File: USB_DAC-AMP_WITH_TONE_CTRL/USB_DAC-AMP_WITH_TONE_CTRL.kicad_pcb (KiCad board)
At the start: 2 copper layers, 9 parts, among them J2 SJ-3524-SMT, U1 PCM2906, U2 TPS61040DBV, U3 SPX3819M5-L, U4 SPX3819M5-L

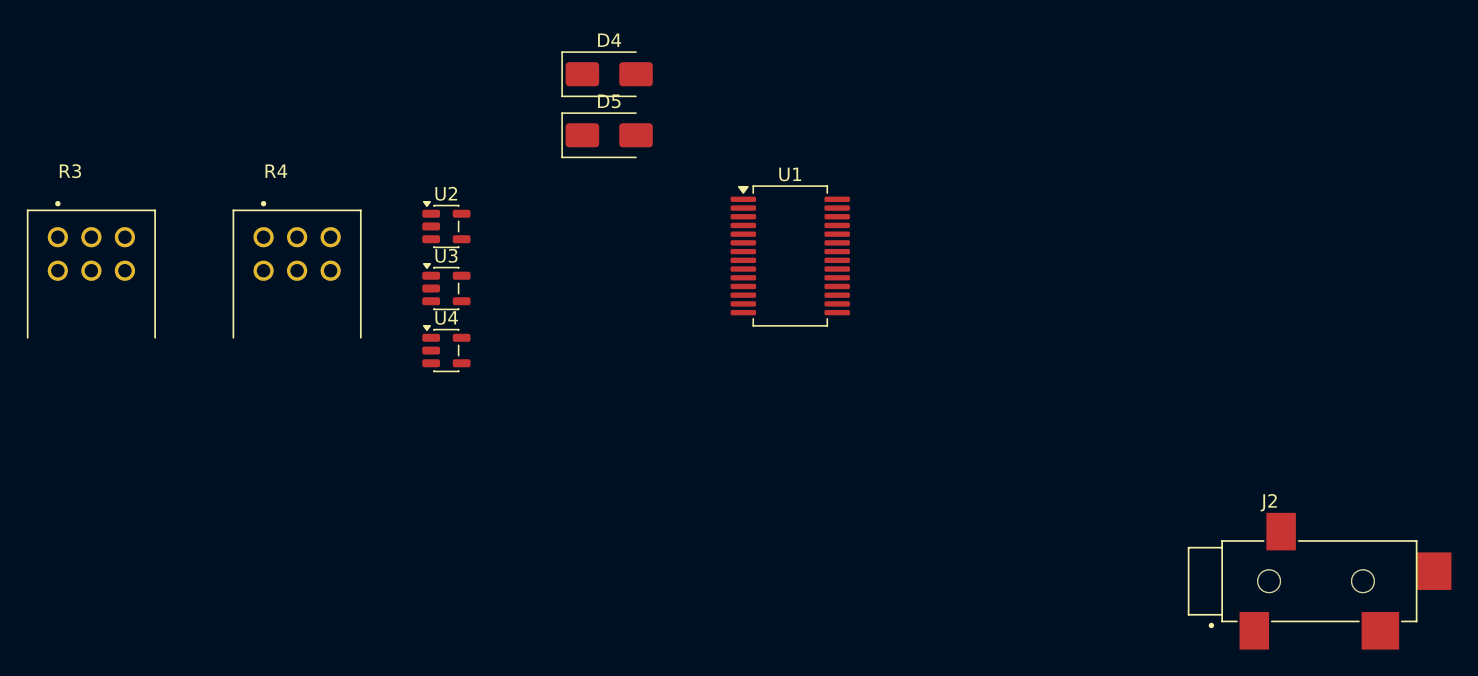
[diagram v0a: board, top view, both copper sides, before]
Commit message: finished USB_DAC-AMP schematic
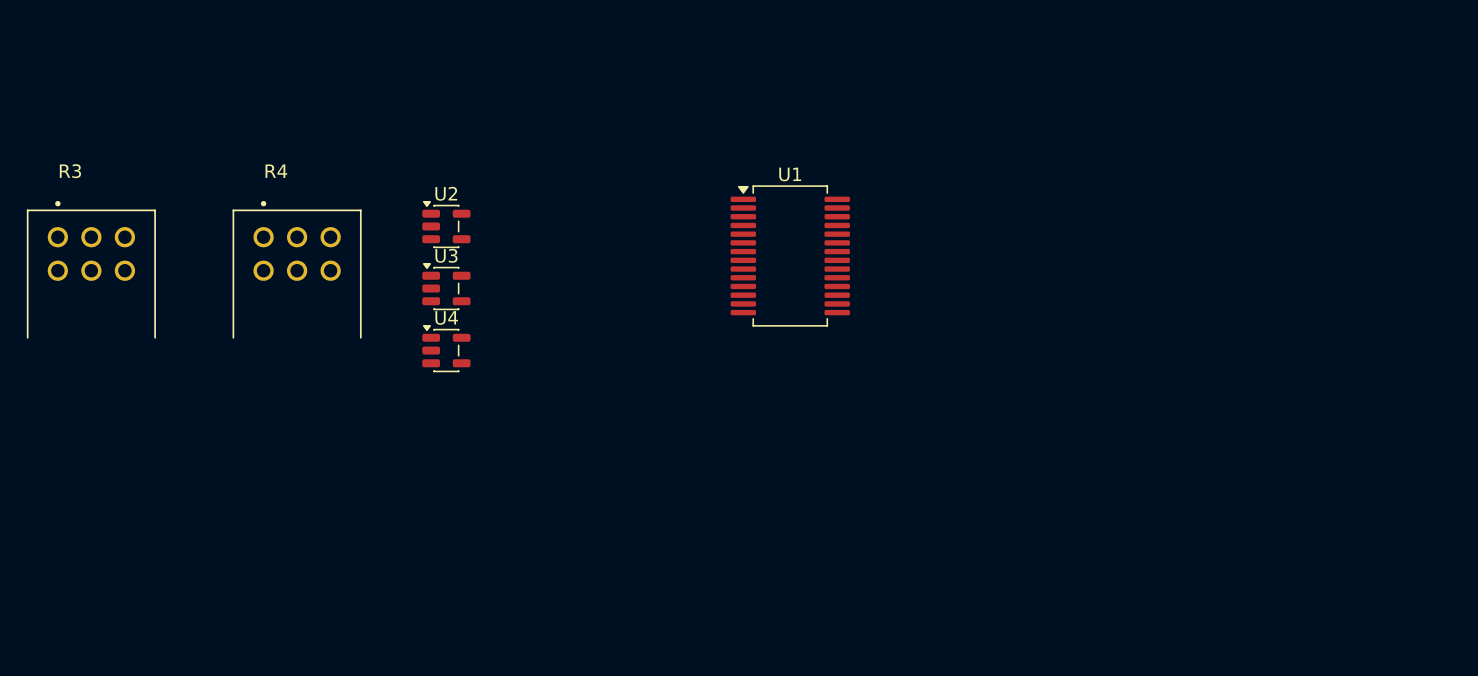
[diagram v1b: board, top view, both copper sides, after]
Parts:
- removed D4, D5: SS14, Diode_SMD:D_SMA
- removed J2: SJ-3524-SMT, Imported_footprints:SJ-3524-SMT
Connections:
- R3 pad 1_1: Net-(C30-Pad2) -> unconnected-(R3-Pad1_1)
- R3 pad 1_2: Net-(C40-Pad2) -> unconnected-(R3-Pad1_2)
- R3 pad 2_1: Net-(C31-Pad2) -> unconnected-(R3-Pad2_1)
- R3 pad 2_2: Net-(C41-Pad2) -> unconnected-(R3-Pad2_2)
- R3 pad 3_1: Net-(U7A-+) -> unconnected-(R3-Pad3_1)
- R3 pad 3_2: Net-(U11A-+) -> unconnected-(R3-Pad3_2)
- U1 pad 1: Net-(U1-D+) -> unconnected-(U1-D+-Pad1)
- U1 pad 10: Net-(D5-K) -> unconnected-(U1-VCCCI-Pad10)
- U1 pad 12: Net-(U1-VINL) -> unconnected-(U1-VINL-Pad12)
- U1 pad 13: Net-(U1-VINR) -> unconnected-(U1-VINR-Pad13)
- U1 pad 14: Net-(U1-VCOM) -> unconnected-(U1-VCOM-Pad14)
- U1 pad 15: /VOUTR -> unconnected-(U1-VOUTR-Pad15)
- U1 pad 16: /VOUTL -> unconnected-(U1-VOUTL-Pad16)
- U1 pad 17: Net-(U1-VCCP1I) -> unconnected-(U1-VCCP1I-Pad17)
- U1 pad 19: Net-(U1-VCCP2I) -> unconnected-(U1-VCCP2I-Pad19)
- U1 pad 2: Net-(U1-D-) -> unconnected-(U1-D--Pad2)
- U1 pad 20: Net-(U1-XTO) -> unconnected-(U1-XTO-Pad20)
- U1 pad 21: Net-(U1-XTI) -> unconnected-(U1-XTI-Pad21)
- U1 pad 23: Net-(U1-VCCXI) -> unconnected-(U1-VCCXI-Pad23)
- U1 pad 24: Net-(U1-DIN) -> unconnected-(U1-DIN-Pad24)
- U1 pad 27: VDDI -> unconnected-(U1-VDDI-Pad27)
- U1 pad 28: Net-(U1-~{SSPND}) -> unconnected-(U1-~{SSPND}-Pad28)
- U1 pad 3: Net-(U1-VBUS) -> unconnected-(U1-VBUS-Pad3)
- U1 pad 5: Net-(U1-HID0) -> unconnected-(U1-HID0-Pad5)
- U1 pad 8: VDDI -> unconnected-(U1-SEL0-Pad8)
- U1 pad 9: VDDI -> unconnected-(U1-SEL1-Pad9)
- U2 pad 1: Net-(D4-A) -> unconnected-(U2-SW-Pad1)
- U2 pad 2: GND -> unconnected-(U2-GND-Pad2)
- U2 pad 3: Net-(U2-FB) -> unconnected-(U2-FB-Pad3)
- U2 pad 4: +5V -> unconnected-(U2-EN-Pad4)
- U2 pad 5: +5V -> unconnected-(U2-VIN-Pad5)
- U3 pad 1: Net-(U3-EN) -> unconnected-(U3-IN-Pad1)
- U3 pad 2: GND -> unconnected-(U3-GND-Pad2)
- U3 pad 3: Net-(U3-EN) -> unconnected-(U3-EN-Pad3)
- U3 pad 4: Net-(U3-ADJ) -> unconnected-(U3-ADJ-Pad4)
- U3 pad 5: +3.7V -> unconnected-(U3-OUT-Pad5)
- U4 pad 1: +16VA -> unconnected-(U4-IN-Pad1)
- U4 pad 2: GND -> unconnected-(U4-GND-Pad2)
- U4 pad 3: +16VA -> unconnected-(U4-EN-Pad3)
- U4 pad 4: Net-(U4-ADJ) -> unconnected-(U4-ADJ-Pad4)
- U4 pad 5: +15V -> unconnected-(U4-OUT-Pad5)
